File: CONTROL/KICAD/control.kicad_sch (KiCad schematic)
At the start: 0 parts

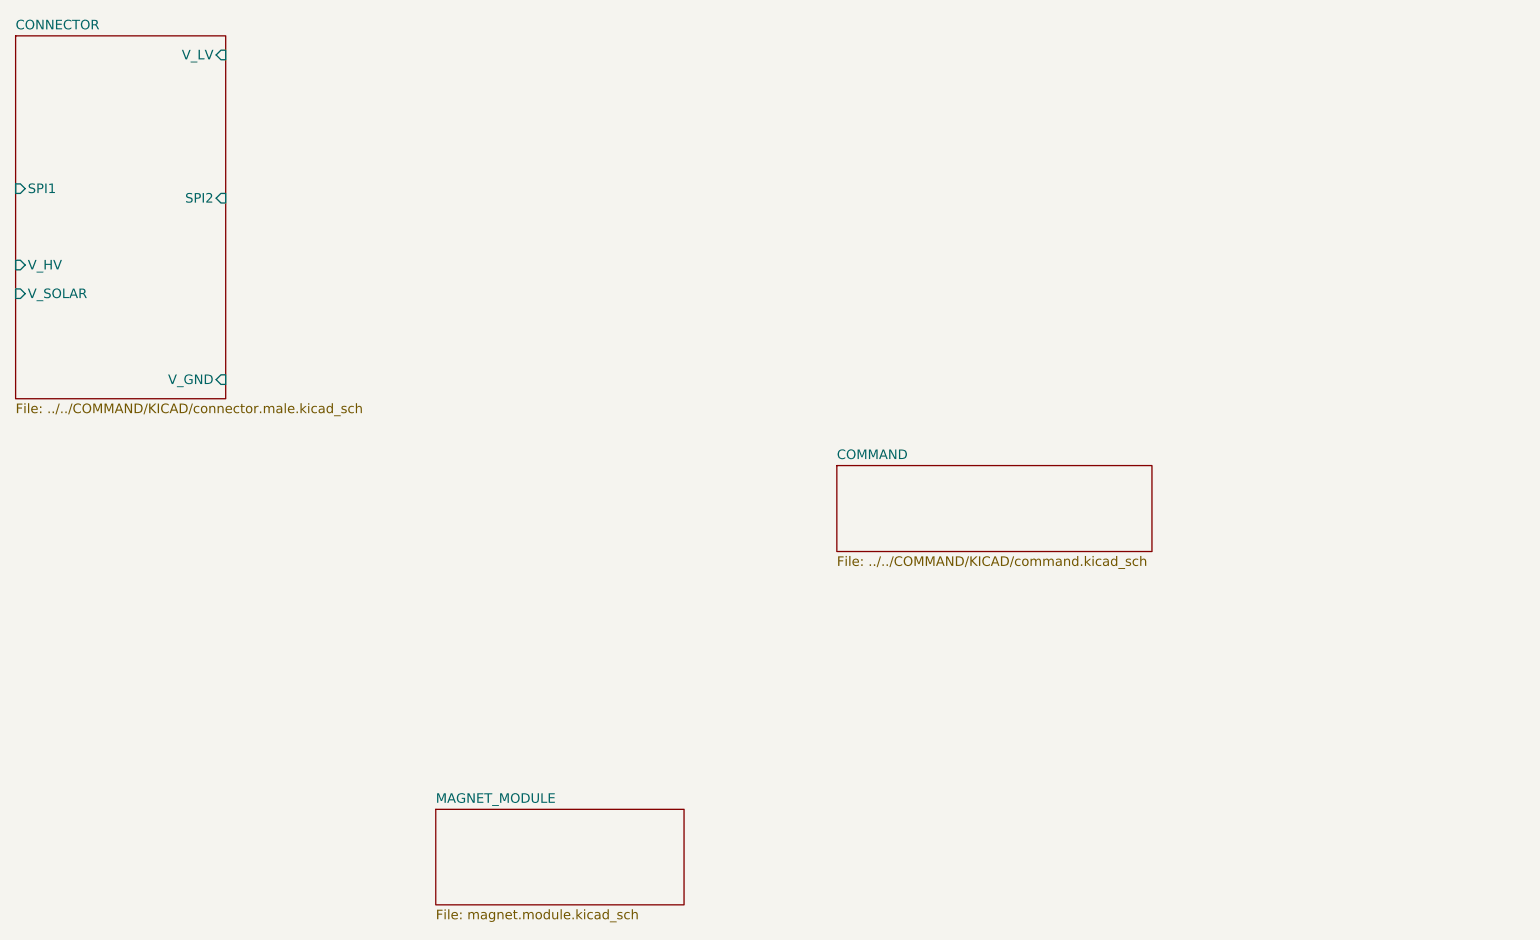
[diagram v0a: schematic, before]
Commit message: Edited Schematics
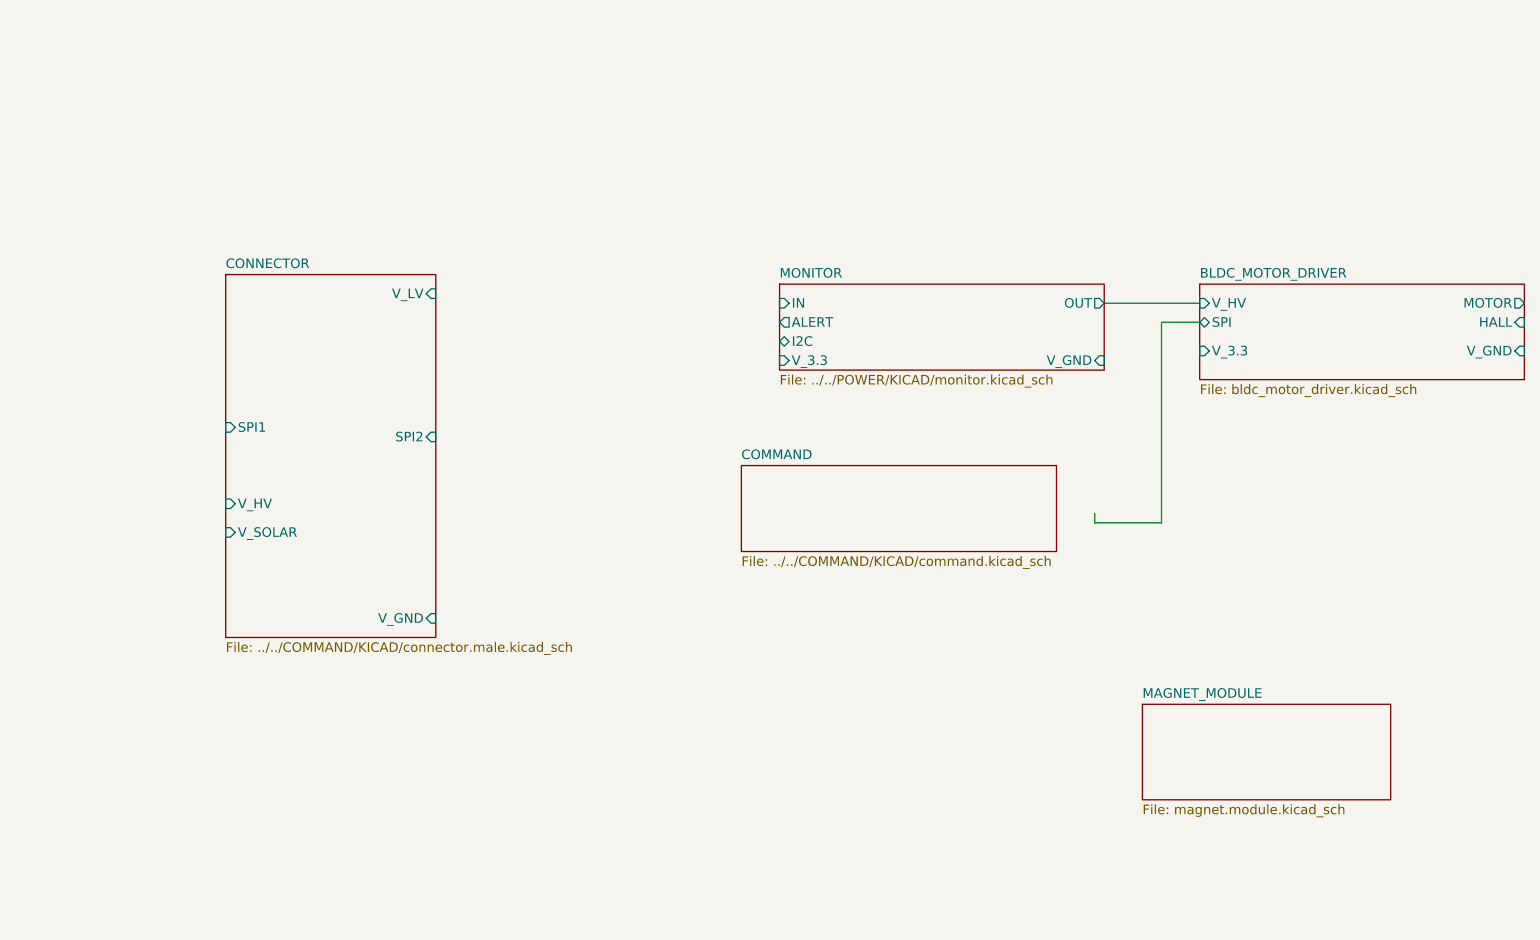
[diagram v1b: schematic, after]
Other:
- added sheet BLDC_MOTOR_DRIVER (bldc_motor_driver.kicad_sch)
- added sheet MONITOR (../../POWER/KICAD/monitor.kicad_sch)

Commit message: Updated Control PCB / Schematics
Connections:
- no-connect marks 0 -> 2
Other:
- sheet CONNECTOR renamed CONNECTOR_X+
- removed sheet BLDC_MOTOR_DRIVER
- removed sheet COMMAND
- removed sheet MAGNET_MODULE
- removed sheet MONITOR
- added sheet MAGNETORQUERS (magnetorquers.kicad_sch)
- added sheet REACTION WHEELS (reaction_wheels.kicad_sch)
- sheet CONNECTOR_X+: file ../../COMMAND/KICAD/connector.male.kicad_sch -> ../../BUS/KICAD/connector.male.kicad_sch
- sheet CONNECTOR_X+ ports: added CAN, CAN{H L}, I2C, I2C_A{SCL SDA}, I2C_B{SCL SDA}, MAGNET, RESET, SHUTDOWN, USB{DP DM}, V_3.3A, V_3.3B, V_BAT; removed SPI1, SPI2, V_HV, V_LV
- note added: "ENABLE TURNS ON THE SPI GATE DRIVER FOR THIS ALONG WITH THE FUSE"
- note added: "MOSI = SDI MISO = SDO"

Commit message: schematic design
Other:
- sheet CONNECTOR_X+ ports: added {CAN}, {I2C}, {USB}; removed CAN, CAN{H L}, I2C, USB{DP DM}
- sheet MAGNETORQUERS ports: added V_3.3, V_GND, {CAN}, {I2C}; removed none
- sheet REACTION WHEELS ports: added {CAN}, {I2C}; removed CAN, I2C
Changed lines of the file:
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@@
 	(paper "A4")
 	(bus_alias "CONTROL"
-		(members "BRAKE" "PWM" "FAULT" "SLEEP" "DRVOFF" "FGOUT}")
+		(members "BRAKE" "PWM" "FAULT" "SLEEP" "DRVOFF" "FGOUT")
 	)
 	(bus_alias "I2C"
@@
 		)
 	)
+	(wire
+		(pts
+			(xy 172.72 107.95) (xy 170.18 107.95)
+		)
+		(stroke
+			(width 0)
+			(type default)
+		)
+	)
 	(bus
 		(pts
@@
 			)
 			(justify right bottom)
+		)
+	)
+	(symbol
+		(lib_id "power:GND")
+		(at 172.72 107.95 90)
+		(unit 1)
+		(exclude_from_sim no)
+		(in_bom yes)
+		(on_board yes)
+		(dnp no)
+		(fields_autoplaced yes)
+		(property "Reference" "#PWR06"
+			(at 179.07 107.95 0)
+			(effects
+				(font
+					(size 1.27 1.27)
+				)
+				(hide yes)
+			)
+		)
+		(property "Value" "GND"
+			(at 176.53 107.9499 90)
+			(effects
+				(font
+					(size 1.27 1.27)
+				)
+				(justify right)
+			)
+		)
+		(property "Footprint" ""
+			(at 172.72 107.95 0)
+			(effects
+				(font
+					(size 1.27 1.27)
+				)
+				(hide yes)
+			)
+		)
+		(property "Datasheet" ""
+			(at 172.72 107.95 0)
+			(effects
+				(font
+					(size 1.27 1.27)
+				)
+				(hide yes)
+			)
+		)
+		(property "Description" "Power symbol creates a global label with name \"GND\" , ground"
+			(at 172.72 107.95 0)
+			(effects
+				(font
+					(size 1.27 1.27)
+				)
+				(hide yes)
+			)
+		)
+		(pin "1"
+		)
+		(instances
+			(project "control"
+				(path "/c4b3c8f9-82bd-4648-8d22-870bf16aa829"
+					(reference "#PWR06")
+					(unit 1)
+				)
+			)
 		)
 	)
@@
 			)
 		)
+		(pin "V_GND" input
+			(at 170.18 107.95 0)
+			(effects
+				(font
+					(size 1.27 1.27)
+				)
+				(justify right)
+			)
+		)
+		(pin "V_3.3" input
+			(at 170.18 92.71 0)
+			(effects
+				(font
+					(size 1.27 1.27)
+				)
+				(justify right)
+			)
+		)
+		(pin "{I2C}" bidirectional
+			(at 115.57 96.52 180)
+			(effects
+				(font
+					(size 1.27 1.27)
+				)
+				(justify left)
+			)
+		)
+		(pin "{CAN}" bidirectional
+			(at 115.57 93.98 180)
+			(effects
+				(font
+					(size 1.27 1.27)
+				)
+				(justify left)
+			)
+		)
 		(instances
 			(project "control"
@@
 			)
 		)
-		(pin "CAN" bidirectional
+		(pin "{CAN}" bidirectional
 			(at 115.57 60.96 180)
 			(effects
@@
 			)
 		)
-		(pin "I2C" bidirectional
+		(pin "{I2C}" bidirectional
 			(at 115.57 63.5 180)
 			(effects
@@
 			)
 		)
-		(pin "CAN" bidirectional
+		(pin "{CAN}" bidirectional
 			(at 40.64 93.98 0)
 			(effects
@@
 			)
 		)
-		(pin "I2C" bidirectional
+		(pin "{I2C}" bidirectional
 			(at 40.64 96.52 0)
 			(effects
@@
 			)
 		)
-		(pin "CAN{H L}" bidirectional
-			(at 40.64 74.93 0)
-			(effects
-				(font
-					(size 1.27 1.27)
-				)
-				(justify right)
-			)
-		)
-		(pin "USB{DP DM}" bidirectional
+		(pin "{USB}" bidirectional
 			(at 40.64 72.39 0)
 			(effects
